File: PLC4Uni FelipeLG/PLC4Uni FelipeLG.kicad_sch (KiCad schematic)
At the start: 6 parts, among them J1 Screw_Terminal_01x02, J2 Screw_Terminal_01x09, J3 Screw_Terminal_01x02, J4 Screw_Terminal_01x02, J5 Screw_Terminal_01x03, J6 Screw_Terminal_01x09

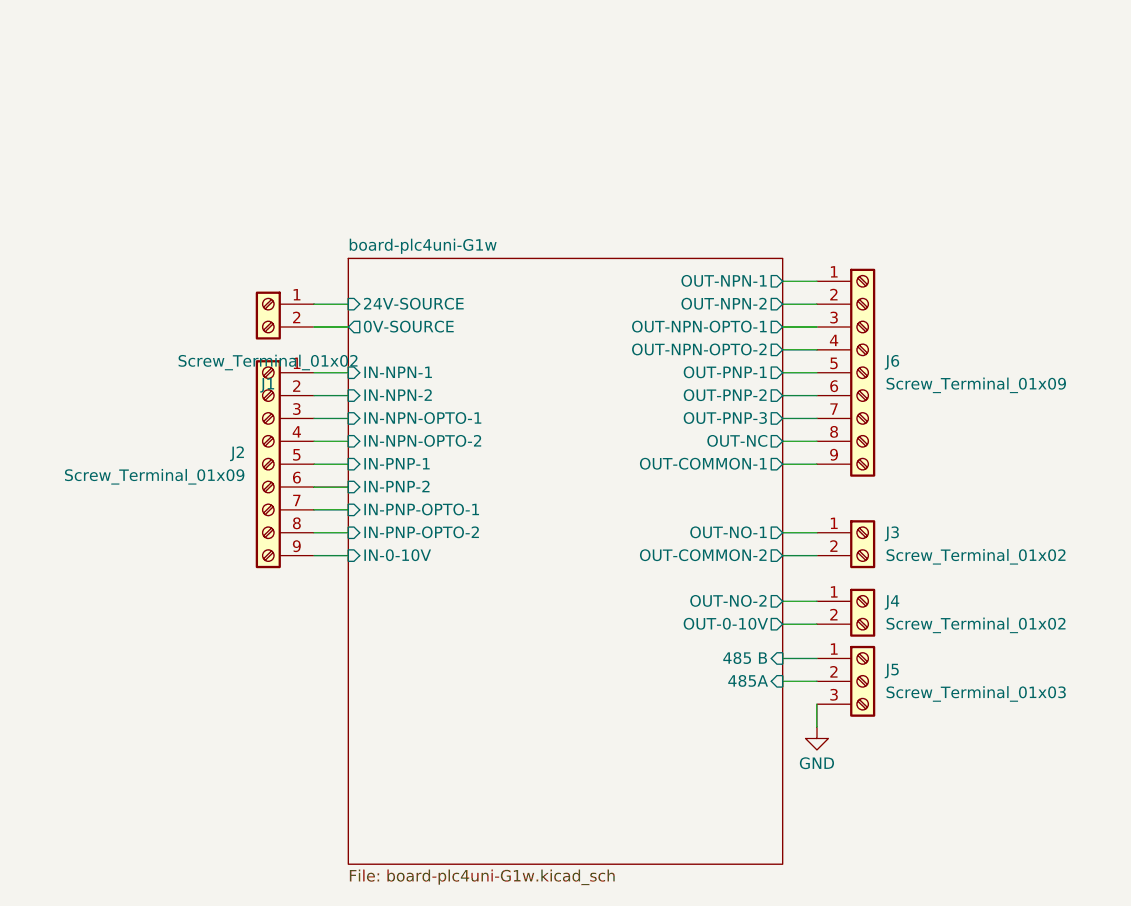
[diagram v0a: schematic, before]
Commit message: Add files via upload
Updated Circuitos corregidos y pistas agregadas
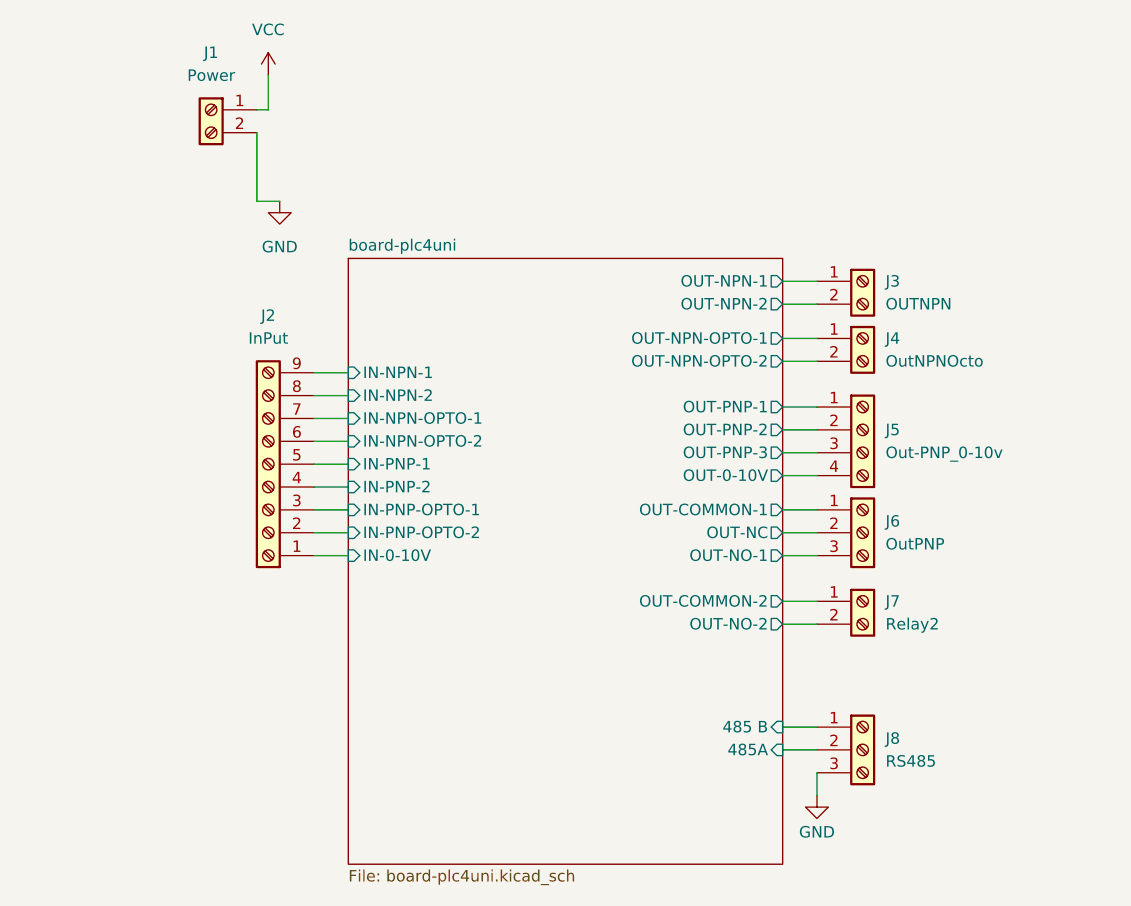
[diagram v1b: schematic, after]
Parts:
- removed J6: Screw_Terminal_01x09, TerminalBlock_Phoenix:TerminalBlock_Phoenix_PT-1,5-9-5.0-H_1x09_P5.00mm_Horizontal, symbol Connector:Screw_Terminal_01x09
- added J5: Out-PNP_0-10v, TerminalBlock_Phoenix:TerminalBlock_Phoenix_PT-1,5-4-5.0-H_1x04_P5.00mm_Horizontal, symbol Connector:Screw_Terminal_01x04
- added J6: OutPNP, TerminalBlock_Phoenix:TerminalBlock_Phoenix_PT-1,5-3-5.0-H_1x03_P5.00mm_Horizontal, symbol Connector:Screw_Terminal_01x03
- added J7: Relay2, TerminalBlock_Phoenix:TerminalBlock_Phoenix_PT-1,5-2-5.0-H_1x02_P5.00mm_Horizontal, symbol Connector:Screw_Terminal_01x02
- J1: value Screw_Terminal_01x02 -> Power
- J2: value Screw_Terminal_01x09 -> InPut
- J3: value Screw_Terminal_01x02 -> OUTNPN
- J4: value Screw_Terminal_01x02 -> OutNPNOcto
- J8: renamed from J5; value Screw_Terminal_01x03 -> RS485
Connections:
- net board-plc4uni/0V-SOURCE is gone; now on net GND: J1.2 (Pin_2)
- net board-plc4uni/IN-0-10V: now also J2.1 (Pin_1); no longer J2.9 (Pin_9)
- net board-plc4uni/IN-NPN-1: now also J2.9 (Pin_9); no longer J2.1 (Pin_1)
- net board-plc4uni/IN-NPN-2: now also J2.8 (Pin_8); no longer J2.2 (Pin_2)
- net board-plc4uni/IN-NPN-OPTO-1: now also J2.7 (Pin_7); no longer J2.3 (Pin_3)
- net board-plc4uni/IN-NPN-OPTO-2: now also J2.6 (Pin_6); no longer J2.4 (Pin_4)
- net board-plc4uni/IN-PNP-2: now also J2.4 (Pin_4); no longer J2.6 (Pin_6)
- net board-plc4uni/IN-PNP-OPTO-1: now also J2.3 (Pin_3); no longer J2.7 (Pin_7)
- net board-plc4uni/IN-PNP-OPTO-2: now also J2.2 (Pin_2); no longer J2.8 (Pin_8)
- net board-plc4uni/OUT-0-10V: now also J5.4 (Pin_4); no longer J4.2 (Pin_2)
- net board-plc4uni/OUT-COMMON-1: now also J6.1 (Pin_1)
- net board-plc4uni/OUT-COMMON-2: now also J7.1 (Pin_1); no longer J3.2 (Pin_2)
- net board-plc4uni/OUT-NC: now also J6.2 (Pin_2)
- net board-plc4uni/OUT-NO-1: now also J6.3 (Pin_3); no longer J3.1 (Pin_1)
- net board-plc4uni/OUT-NO-2: now also J7.2 (Pin_2); no longer J4.1 (Pin_1)
- net board-plc4uni/OUT-NPN-1: now also J3.1 (Pin_1)
- net board-plc4uni/OUT-NPN-2: now also J3.2 (Pin_2)
- net board-plc4uni/OUT-NPN-OPTO-1: now also J4.1 (Pin_1)
- net board-plc4uni/OUT-NPN-OPTO-2: now also J4.2 (Pin_2)
- net board-plc4uni/OUT-PNP-1: now also J5.1 (Pin_1)
- net board-plc4uni/OUT-PNP-2: now also J5.2 (Pin_2)
- net board-plc4uni/OUT-PNP-3: now also J5.3 (Pin_3)
- net board-plc4uni/24V-SOURCE renamed VCC
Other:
- sheet board-plc4uni-G1w renamed board-plc4uni
- sheet board-plc4uni: file board-plc4uni-G1w.kicad_sch -> board-plc4uni.kicad_sch
- sheet board-plc4uni ports: added none; removed 0V-SOURCE, 24V-SOURCE
- moved on the sheet: J1, J2, J3, J4, J8
